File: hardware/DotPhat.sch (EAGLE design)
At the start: 22 parts, among them CN1 1X4-BIG, J2 RASPBERRYPI-40-PIN-GPIO_PTH, J3 USB-MICROB, U1 ATMEGA328P-MU-QFN32, X3 S4B-ZR

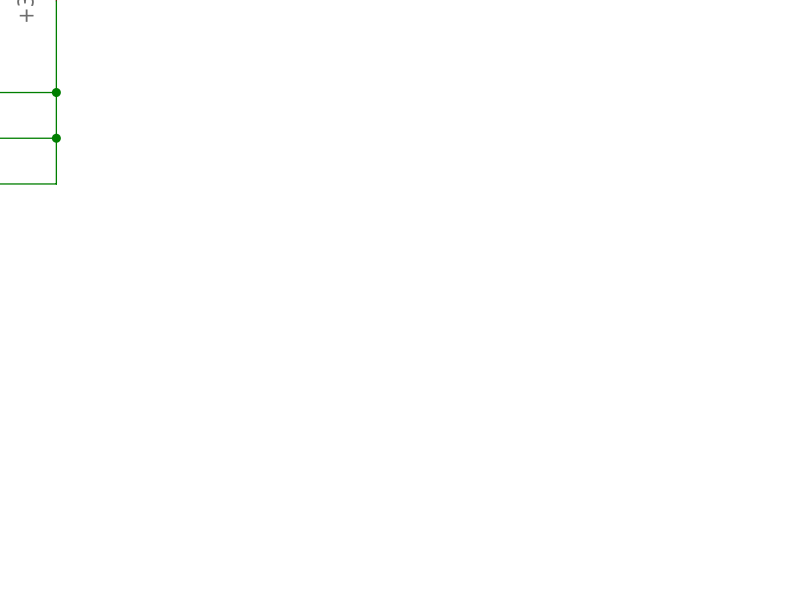
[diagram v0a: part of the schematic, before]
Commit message: Add mandatory 5V-3.3V capless regulator for USB power
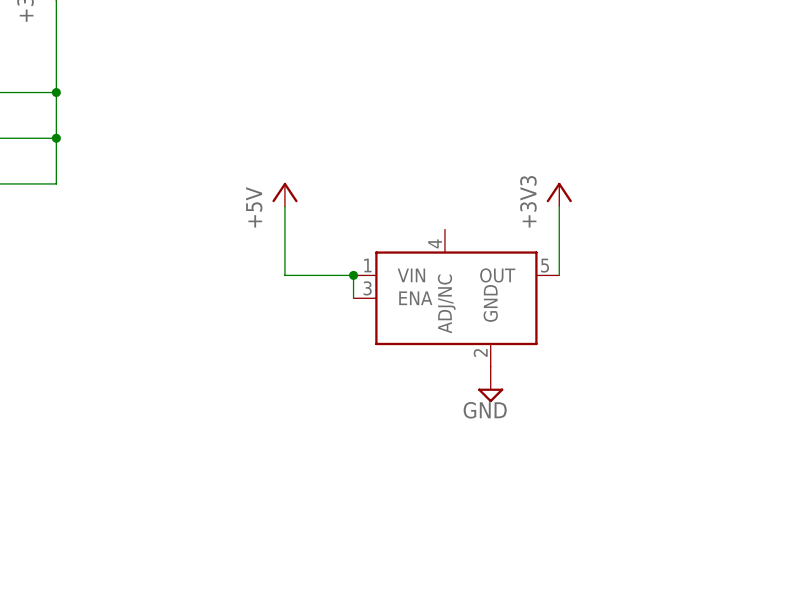
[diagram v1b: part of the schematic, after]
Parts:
- added U$4: LDCL015, LDCL015:LDCL015
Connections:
- net +3V3: now also U$4.OUT
- net +5V: now also U$4.ENA, U$4.VIN
- net GND: now also U$4.GND
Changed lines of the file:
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@@
 <part name="LED5" library="SparkFun" deviceset="LED" device="0603"/>
 <part name="SUPPLY12" library="supply2" deviceset="GND" device=""/>
+<part name="U$4" library="LDCL015" deviceset="LDCL015" device=""/>
+<part name="SUPPLY27" library="supply2" deviceset="GND" device=""/>
+<part name="+3V19" library="supply1" deviceset="+3V3" device=""/>
+<part name="P+4" library="supply1" deviceset="+5V" device=""/>
 </parts>
 <sheets>
@@
 <instance part="LED5" gate="G$1" x="129.54" y="152.4" rot="R90"/>
 <instance part="SUPPLY12" gate="GND" x="160.02" y="152.4" rot="R90"/>
+<instance part="U$4" gate="G$1" x="144.78" y="-38.1"/>
+<instance part="SUPPLY27" gate="GND" x="149.86" y="-48.26" rot="MR0"/>
+<instance part="+3V19" gate="G$1" x="157.48" y="-25.4"/>
+<instance part="P+4" gate="1" x="127" y="-25.4"/>
 </instances>
 <busses>
@@
 <wire x1="106.68" y1="125.73" x2="100.33" y2="125.73" width="0.1524" layer="91"/>
 </segment>
+<segment>
+<pinref part="U$4" gate="G$1" pin="GND"/>
+<pinref part="SUPPLY27" gate="GND" pin="GND"/>
+</segment>
 </net>
 <net name="SDA" class="0">
@@
 <pinref part="+3V7" gate="G$1" pin="+3V3"/>
 </segment>
+<segment>
+<pinref part="U$4" gate="G$1" pin="OUT"/>
+<pinref part="+3V19" gate="G$1" pin="+3V3"/>
+<wire x1="157.48" y1="-27.94" x2="157.48" y2="-35.56" width="0.1524" layer="91"/>
+</segment>
 </net>
 <net name="ADCENA" class="0">
@@
 <pinref part="J3" gate="G$1" pin="VBUS"/>
 </segment>
-</net>
+<segment>
+<pinref part="P+4" gate="1" pin="+5V"/>
+<pinref part="U$4" gate="G$1" pin="VIN"/>
+<wire x1="127" y1="-27.94" x2="127" y2="-35.56" width="0.1524" layer="91"/>
+<wire x1="127" y1="-35.56" x2="134.62" y2="-35.56" width="0.1524" layer="91"/>
+<pinref part="U$4" gate="G$1" pin="ENA"/>
+<wire x1="134.62" y1="-38.1" x2="134.62" y2="-35.56" width="0.1524" layer="91"/>
+<junction x="134.62" y="-35.56"/>
+</segment>
+</net>

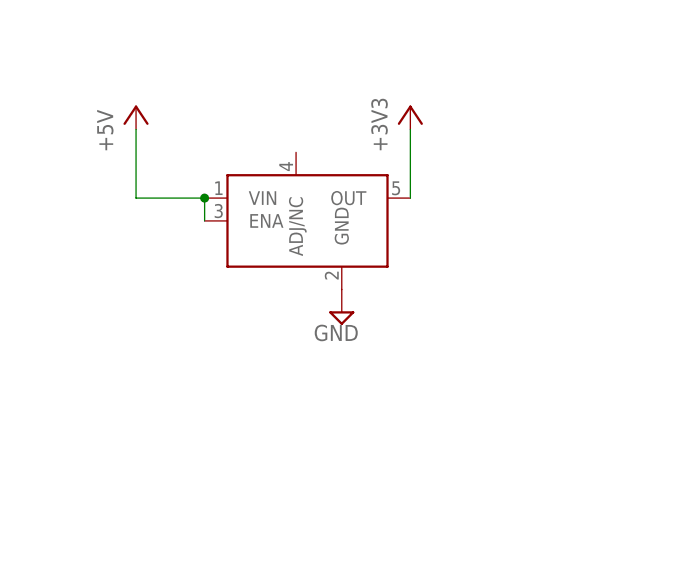
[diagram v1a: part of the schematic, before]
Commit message: Add filter cap at 3.3V regulator out pin
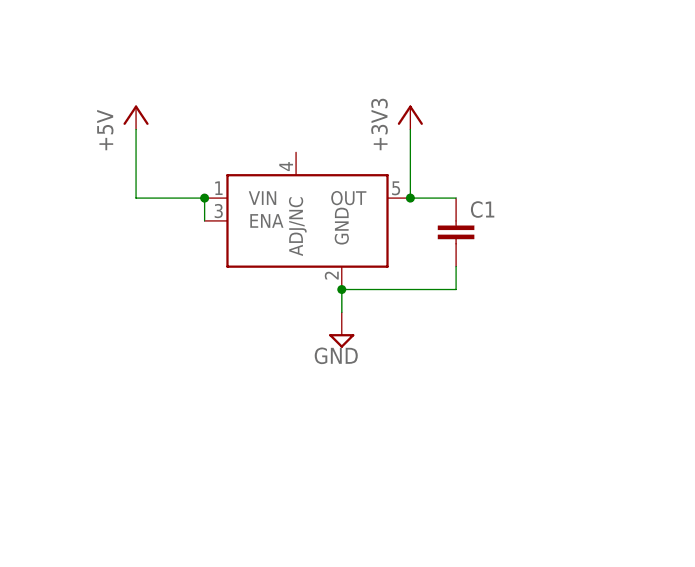
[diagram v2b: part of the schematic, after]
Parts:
- added C1: (no value), rcl:C-EUC0603
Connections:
- net +3V3: now also C1.1
- net GND: now also C1.2
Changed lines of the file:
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@@
 <part name="+3V19" library="supply1" deviceset="+3V3" device=""/>
 <part name="P+4" library="supply1" deviceset="+5V" device=""/>
+<part name="C1" library="rcl" deviceset="C-EU" device="C0603"/>
 </parts>
 <sheets>
@@
 <instance part="SUPPLY12" gate="GND" x="160.02" y="152.4" rot="R90"/>
 <instance part="U$4" gate="G$1" x="144.78" y="-38.1"/>
-<instance part="SUPPLY27" gate="GND" x="149.86" y="-48.26" rot="MR0"/>
+<instance part="SUPPLY27" gate="GND" x="149.86" y="-50.8" rot="MR0"/>
 <instance part="+3V19" gate="G$1" x="157.48" y="-25.4"/>
 <instance part="P+4" gate="1" x="127" y="-25.4"/>
+<instance part="C1" gate="G$1" x="162.56" y="-38.1"/>
 </instances>
 <busses>
@@
 <pinref part="U$4" gate="G$1" pin="GND"/>
 <pinref part="SUPPLY27" gate="GND" pin="GND"/>
+<wire x1="149.86" y1="-48.26" x2="149.86" y2="-45.72" width="0.1524" layer="91"/>
+<pinref part="C1" gate="G$1" pin="2"/>
+<wire x1="149.86" y1="-45.72" x2="162.56" y2="-45.72" width="0.1524" layer="91"/>
+<wire x1="162.56" y1="-45.72" x2="162.56" y2="-43.18" width="0.1524" layer="91"/>
+<junction x="149.86" y="-45.72"/>
 </segment>
 </net>
@@
 <pinref part="+3V19" gate="G$1" pin="+3V3"/>
 <wire x1="157.48" y1="-27.94" x2="157.48" y2="-35.56" width="0.1524" layer="91"/>
-</segment>
-</net>
+<pinref part="C1" gate="G$1" pin="1"/>
+<wire x1="162.56" y1="-35.56" x2="157.48" y2="-35.56" width="0.1524" layer="91"/>
+<junction x="157.48" y="-35.56"/>
+</segment>
+</net>

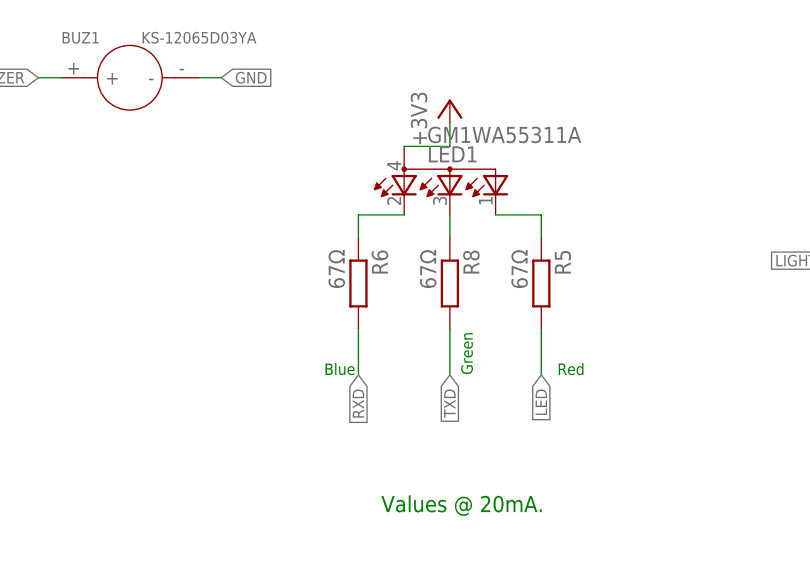
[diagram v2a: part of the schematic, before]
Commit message: Replace RGB resistors for array
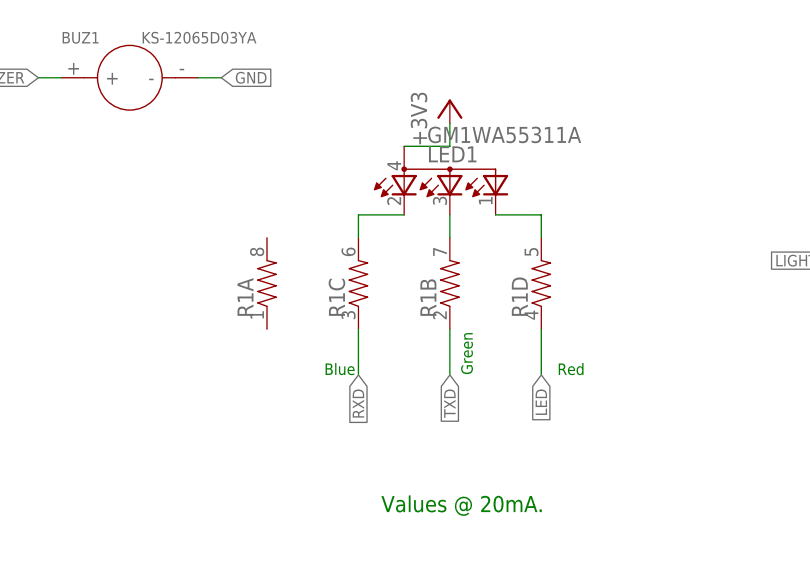
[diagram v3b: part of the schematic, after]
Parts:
- removed R5, R6, R8: 67Ω, resistor:R-EU_R0603
- added R1: (no value), SparkFun:RESISTOR-ARRAY0603-ARV
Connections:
- net LED: now also R1D.1; no longer R5.2
- net N$1: now also R1B.2; no longer R8.1
- net N$15: now also R1D.2; no longer R5.1
- net N$4: now also R1C.2; no longer R6.1
- net RXD: now also R1C.1; no longer R6.2
- net TXD: now also R1B.1; no longer R8.2
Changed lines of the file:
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@@
 <part name="Y1" library="SparkFun-Clocks" deviceset="RESONATOR" device="SMD-3.2X1.3"/>
 <part name="SUPPLY30" library="supply2" deviceset="GND" device=""/>
-<part name="R5" library="resistor" deviceset="R-EU_" device="R0603" value="67Ω"/>
-<part name="R6" library="resistor" deviceset="R-EU_" device="R0603" value="67Ω"/>
-<part name="R8" library="resistor" deviceset="R-EU_" device="R0603" value="67Ω"/>
 <part name="+3V14" library="supply1" deviceset="+3V3" device=""/>
 <part name="LED1" library="led" deviceset="GM1WA55311A" device=""/>
@@
 <part name="P+4" library="supply1" deviceset="+5V" device=""/>
 <part name="C1" library="rcl" deviceset="C-EU" device="C0603"/>
+<part name="R1" library="SparkFun" deviceset="RESISTOR-ARRAY" device="0603-ARV"/>
 </parts>
 <sheets>
@@
 <instance part="Y1" gate="G$1" x="81.28" y="68.58" rot="R90"/>
 <instance part="SUPPLY30" gate="GND" x="88.9" y="66.04"/>
-<instance part="R5" gate="G$1" x="-12.7" y="60.96" rot="R270"/>
-<instance part="R6" gate="G$1" x="-33.02" y="60.96" rot="R270"/>
-<instance part="R8" gate="G$1" x="-22.86" y="60.96" rot="R270"/>
 <instance part="+3V14" gate="G$1" x="-22.86" y="81.28"/>
 <instance part="LED1" gate="G$1" x="-22.86" y="73.66"/>
@@
 <instance part="P+4" gate="1" x="127" y="-25.4"/>
 <instance part="C1" gate="G$1" x="162.56" y="-38.1"/>
+<instance part="R1" gate="A" x="-43.18" y="60.96" rot="R90"/>
+<instance part="R1" gate="B" x="-22.86" y="60.96" rot="R90"/>
+<instance part="R1" gate="C" x="-33.02" y="60.96" rot="R90"/>
+<instance part="R1" gate="D" x="-12.7" y="60.96" rot="R90"/>
 </instances>
 <busses>
@@
 </segment>
 <segment>
-<pinref part="R5" gate="G$1" pin="2"/>
 <wire x1="-12.7" y1="55.88" x2="-12.7" y2="50.8" width="0.1524" layer="91"/>
 <label x="-12.7" y="50.8" size="1.27" layer="95" rot="R270" xref="yes"/>
+<pinref part="R1" gate="D" pin="1"/>
 </segment>
 </net>
@@
 </segment>
 <segment>
-<pinref part="R8" gate="G$1" pin="2"/>
 <wire x1="-22.86" y1="55.88" x2="-22.86" y2="50.8" width="0.1524" layer="91"/>
 <label x="-22.86" y="50.8" size="1.27" layer="95" rot="R270" xref="yes"/>
+<pinref part="R1" gate="B" pin="1"/>
 </segment>
 <segment>
@@
 </segment>
 <segment>
-<pinref part="R6" gate="G$1" pin="2"/>
 <wire x1="-33.02" y1="55.88" x2="-33.02" y2="50.8" width="0.1524" layer="91"/>
 <label x="-33.02" y="50.8" size="1.27" layer="95" rot="R270" xref="yes"/>
+<pinref part="R1" gate="C" pin="1"/>
 </segment>
 <segment>
@@
 <pinref part="LED1" gate="G$1" pin="CBLUE"/>
 <wire x1="-22.86" y1="68.58" x2="-22.86" y2="66.04" width="0.1524" layer="91"/>
-<pinref part="R8" gate="G$1" pin="1"/>
+<pinref part="R1" gate="B" pin="2"/>
 </segment>
 </net>
@@
 <segment>
 <pinref part="LED1" gate="G$1" pin="CGREEN"/>
-<pinref part="R5" gate="G$1" pin="1"/>
 <wire x1="-12.7" y1="66.04" x2="-12.7" y2="68.58" width="0.1524" layer="91"/>
 <wire x1="-12.7" y1="68.58" x2="-17.78" y2="68.58" width="0.1524" layer="91"/>
+<pinref part="R1" gate="D" pin="2"/>
 </segment>
 </net>
@@
 <pinref part="LED1" gate="G$1" pin="CRED"/>
 <wire x1="-27.94" y1="68.58" x2="-33.02" y2="68.58" width="0.1524" layer="91"/>
-<pinref part="R6" gate="G$1" pin="1"/>
 <wire x1="-33.02" y1="68.58" x2="-33.02" y2="66.04" width="0.1524" layer="91"/>
-</segment>
-</net>
+<pinref part="R1" gate="C" pin="2"/>
+</segment>
+</net>

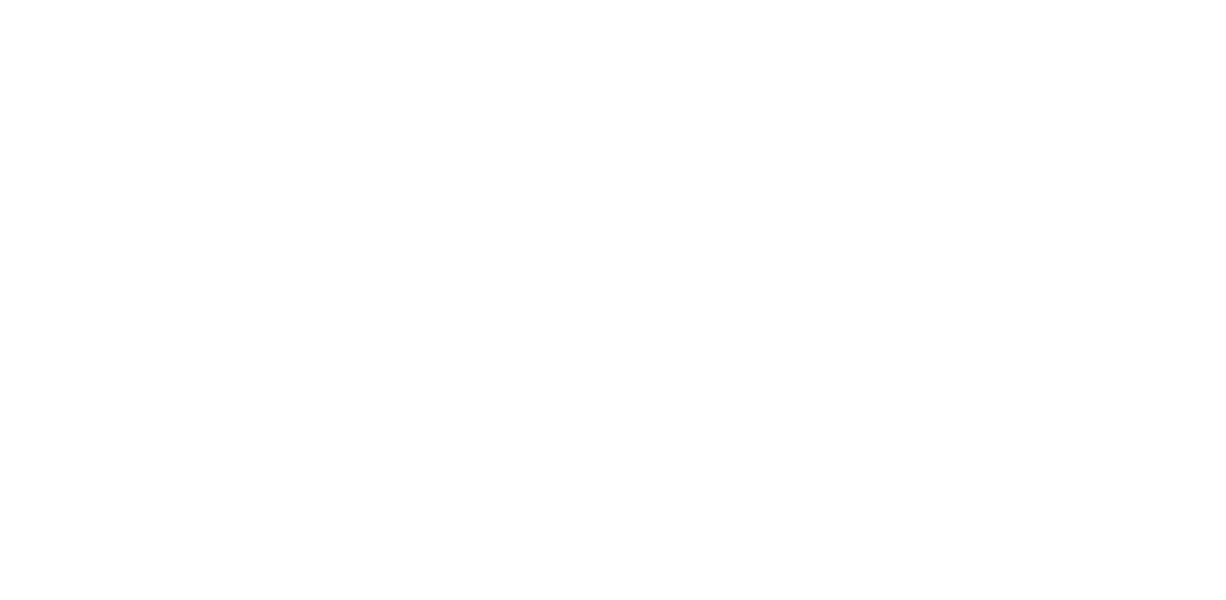
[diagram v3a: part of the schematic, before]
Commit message: Add TMP112 temperature sensor
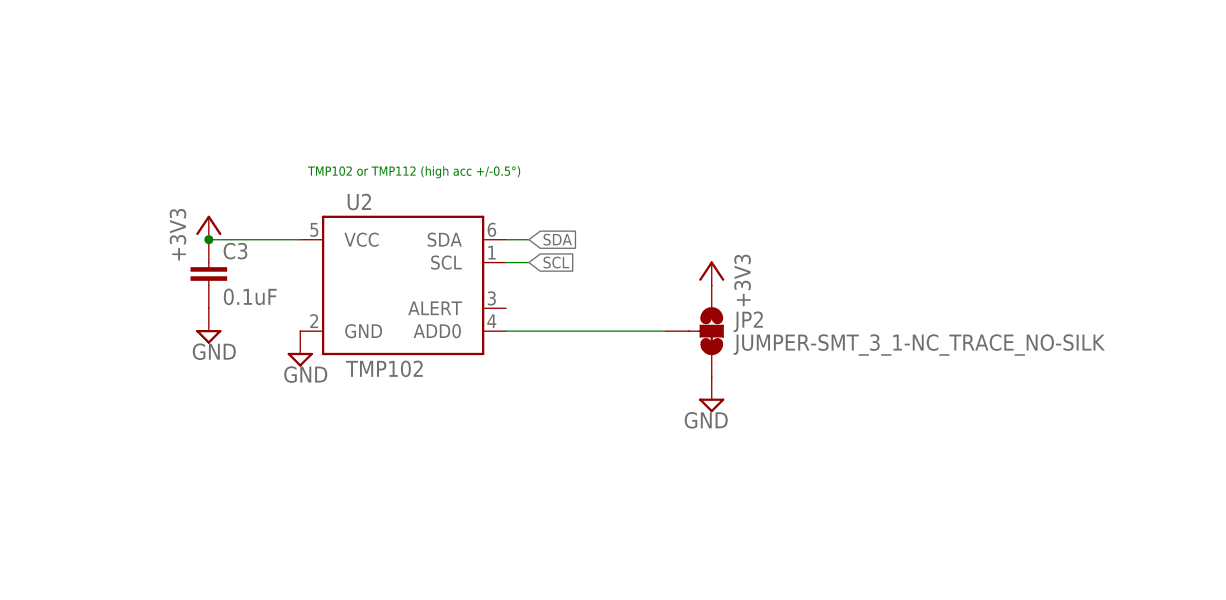
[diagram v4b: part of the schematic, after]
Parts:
- added C3: 0.1uF, resistor:C-EUC0603
- added JP2: JUMPER-SMT_3_1-NC_TRACE_NO-SILK, SparkFun-Jumpers:JUMPER-SMT_3_1-NC_TRACE_NO-SILK
- added U2: TMP102, SparkFun:TMP102
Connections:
- new net N$11: JP2.2, U2.ADD0
- net +3V3: now also C3.1, JP2.1, U2.VCC
- net GND: now also C3.2, JP2.3, U2.GND
- net SCL: now also U2.SCL
- net SDA: now also U2.SDA
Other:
- note added: "TMP102 or TMP112 (high acc +/-0.5°)"
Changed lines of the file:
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@@
 <part name="C1" library="rcl" deviceset="C-EU" device="C0603"/>
 <part name="R1" library="SparkFun" deviceset="RESISTOR-ARRAY" device="0603-ARV"/>
+<part name="U2" library="SparkFun" deviceset="TMP102" device=""/>
+<part name="SUPPLY15" library="supply2" deviceset="GND" device=""/>
+<part name="+3V11" library="supply1" deviceset="+3V3" device=""/>
+<part name="C3" library="resistor" deviceset="C-EU" device="C0603" value="0.1uF"/>
+<part name="SUPPLY13" library="supply2" deviceset="GND" device=""/>
+<part name="SUPPLY17" library="supply2" deviceset="GND" device=""/>
+<part name="+3V12" library="supply1" deviceset="+3V3" device=""/>
+<part name="JP2" library="SparkFun-Jumpers" deviceset="JUMPER-SMT_3_1-NC_TRACE" device="_NO-SILK"/>
 </parts>
 <sheets>
@@
 <text x="-20.32" y="50.8" size="1.27" layer="91" rot="R90">Green</text>
 <text x="-10.922" y="50.8" size="1.27" layer="91">Red</text>
+<text x="228.6" y="20.32" size="1.016" layer="91" align="center">TMP102 or TMP112 (high acc +/-0.5°)</text>
 </plain>
 <instances>
@@
 <instance part="R1" gate="C" x="-33.02" y="60.96" rot="R90"/>
 <instance part="R1" gate="D" x="-12.7" y="60.96" rot="R90"/>
+<instance part="U2" gate="G$1" x="228.6" y="7.62"/>
+<instance part="SUPPLY15" gate="GND" x="215.9" y="0"/>
+<instance part="+3V11" gate="G$1" x="205.74" y="15.24"/>
+<instance part="C3" gate="G$1" x="205.74" y="10.16"/>
+<instance part="SUPPLY13" gate="GND" x="205.74" y="2.54"/>
+<instance part="SUPPLY17" gate="GND" x="261.62" y="-5.08" rot="MR0"/>
+<instance part="+3V12" gate="G$1" x="261.62" y="10.16" rot="MR0"/>
+<instance part="JP2" gate="G$1" x="261.62" y="2.54"/>
 </instances>
 <busses>
@@
 <junction x="149.86" y="-45.72"/>
 </segment>
+<segment>
+<pinref part="U2" gate="G$1" pin="GND"/>
+<pinref part="SUPPLY15" gate="GND" pin="GND"/>
+</segment>
+<segment>
+<pinref part="C3" gate="G$1" pin="2"/>
+<pinref part="SUPPLY13" gate="GND" pin="GND"/>
+</segment>
+<segment>
+<pinref part="SUPPLY17" gate="GND" pin="GND"/>
+<pinref part="JP2" gate="G$1" pin="3"/>
+</segment>
 </net>
 <net name="SDA" class="0">
@@
 <wire x1="76.2" y1="-72.39" x2="68.58" y2="-72.39" width="0.1524" layer="91"/>
 <label x="68.58" y="-72.39" size="1.27" layer="95" rot="R180" xref="yes"/>
+</segment>
+<segment>
+<pinref part="U2" gate="G$1" pin="SDA"/>
+<wire x1="238.76" y1="12.7" x2="241.3" y2="12.7" width="0.1524" layer="91"/>
+<label x="241.3" y="12.7" size="1.27" layer="95" xref="yes"/>
 </segment>
 </net>
@@
 <junction x="157.48" y="-35.56"/>
 </segment>
+<segment>
+<pinref part="+3V11" gate="G$1" pin="+3V3"/>
+<pinref part="C3" gate="G$1" pin="1"/>
+<wire x1="205.74" y1="12.7" x2="215.9" y2="12.7" width="0.1524" layer="91"/>
+<junction x="205.74" y="12.7"/>
+<pinref part="U2" gate="G$1" pin="VCC"/>
+</segment>
+<segment>
+<pinref part="+3V12" gate="G$1" pin="+3V3"/>
+<pinref part="JP2" gate="G$1" pin="1"/>
+</segment>
 </net>
 <net name="ADCENA" class="0">
@@
 <wire x1="76.2" y1="-74.93" x2="68.58" y2="-74.93" width="0.1524" layer="91"/>
 <label x="68.58" y="-74.93" size="1.27" layer="95" rot="R180" xref="yes"/>
+</segment>
+<segment>
+<pinref part="U2" gate="G$1" pin="SCL"/>
+<wire x1="238.76" y1="10.16" x2="241.3" y2="10.16" width="0.1524" layer="91"/>
+<label x="241.3" y="10.16" size="1.27" layer="95" xref="yes"/>
 </segment>
 </net>
@@
 </segment>
 </net>
+<net name="N$11" class="0">
+<segment>
+<pinref part="U2" gate="G$1" pin="ADD0"/>
+<wire x1="256.54" y1="2.54" x2="238.76" y2="2.54" width="0.1524" layer="91"/>
+<pinref part="JP2" gate="G$1" pin="2"/>
+</segment>
+</net>
